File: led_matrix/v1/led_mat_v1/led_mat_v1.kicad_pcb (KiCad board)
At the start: 2 copper layers, 124 parts, among them J1 Left_header, J2 Right_header

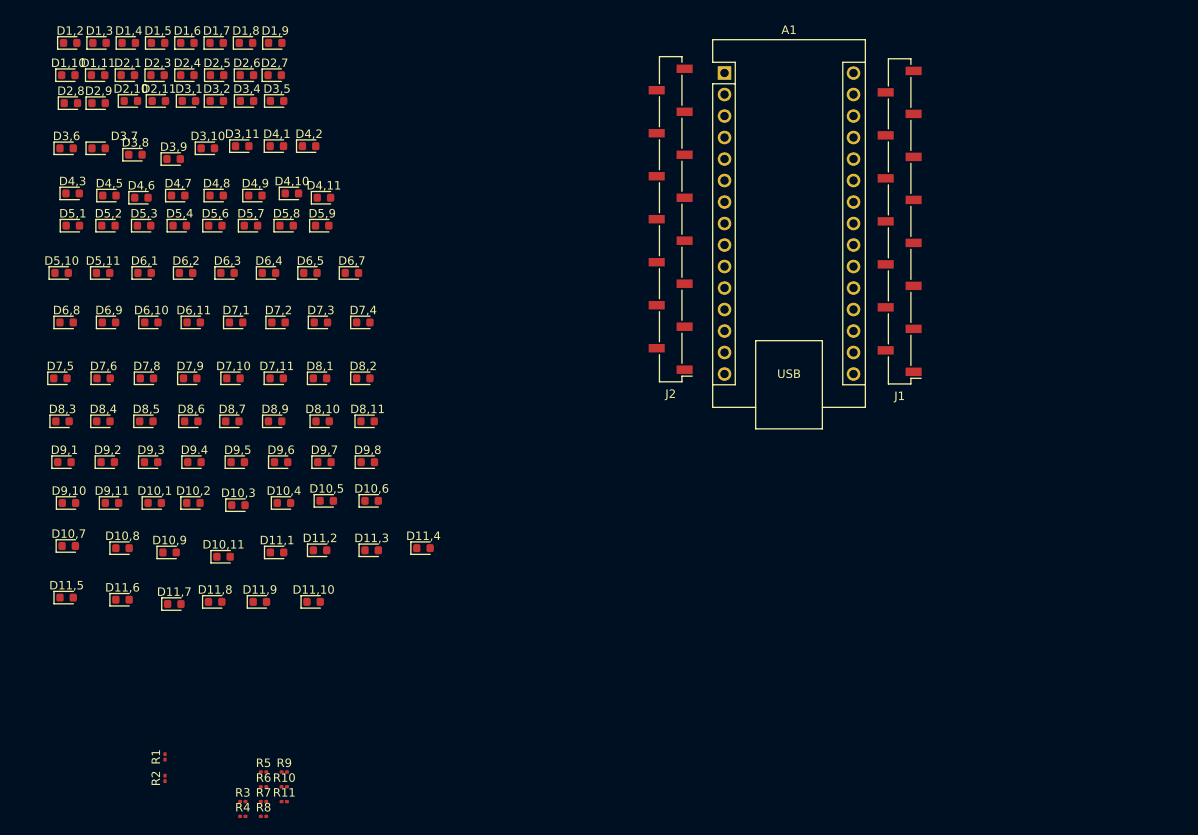
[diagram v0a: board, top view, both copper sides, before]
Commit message: feat(led_matrix): add PCB/schematic exports and update KiCad project files
- Add 3D PCB view export (led_mat_v1.png) and schematic export (led_mat_v1.svg)
- Update schematic, PCB layout, and project files with latest design changes
- Exclude KiCad lock files (*.lck) from version control via .gitignore
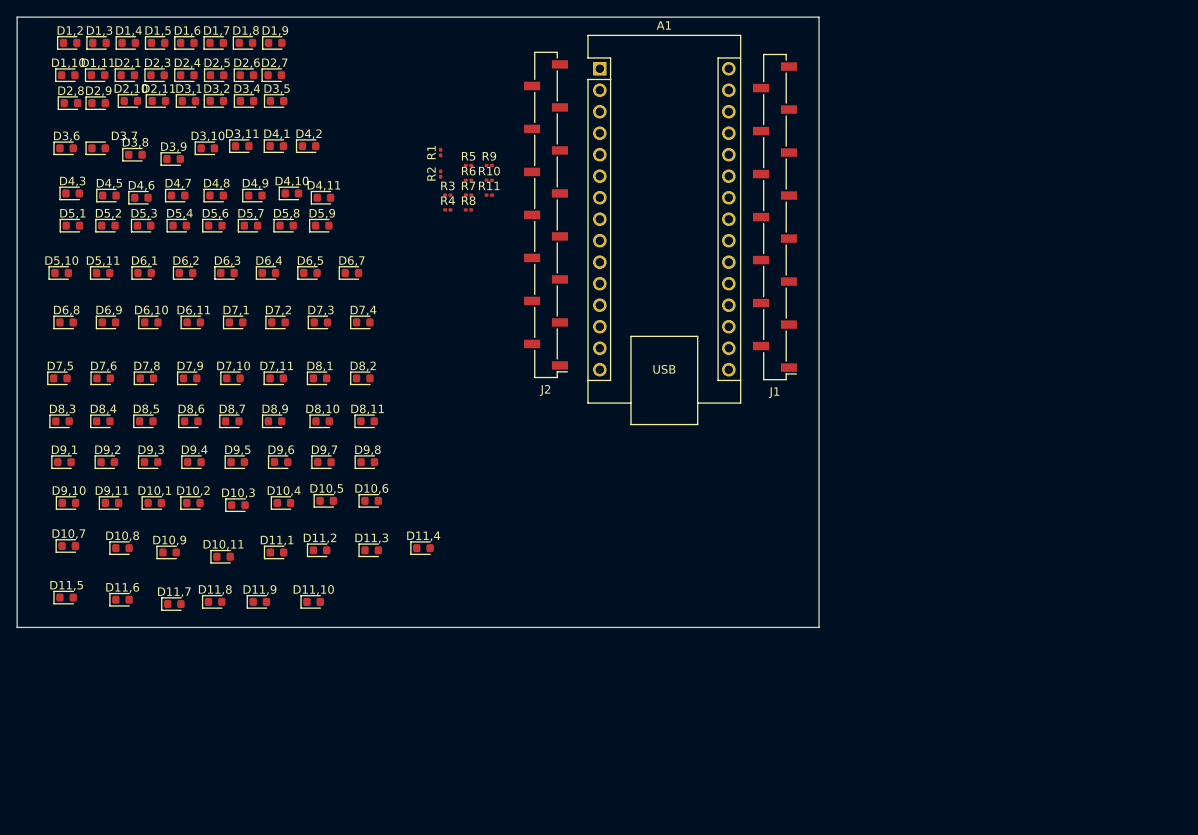
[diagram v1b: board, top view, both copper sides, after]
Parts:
- moved R1 78.5 mm to (105.2, 39.9)
- moved R2 78.5 mm to (105.2, 42.4)
- moved R10 75.6 mm to (110.9, 43.2)
- moved R11 75.6 mm to (110.9, 44.9)
- moved R3 75.6 mm to (106.0, 44.9)
- moved R4 75.6 mm to (106.0, 46.7)
- moved R5 75.6 mm to (108.4, 41.4)
- moved R6 75.6 mm to (108.4, 43.2)
- moved R7 75.6 mm to (108.4, 44.9)
- moved R8 75.6 mm to (108.4, 46.7)
- moved R9 75.6 mm to (110.9, 41.4)
- moved J1 14.7 mm to (144.7, 47.5)
- moved J2 14.7 mm to (117.6, 47.2)
- moved A1 14.7 mm to (124.0, 30.0)
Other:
- board outline added: 94.7 x 72.1 mm
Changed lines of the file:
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@@
 	(footprint "Resistor_SMD:R_0201_0603Metric"
 		(layer "F.Cu")
-		(at 86.68 114.808)
+		(at 110.898 43.152)
 		(descr "Resistor SMD 0201 (0603 Metric), square (rectangular) end terminal, IPC-7351 nominal, (Body size source: https://www.vishay.com/docs/20052/crcw0201e3.pdf)")
 		(tags "resistor")
@@
 	(footprint "Resistor_SMD:R_0201_0603Metric"
 		(layer "F.Cu")
-		(at 84.23 116.558)
+		(at 108.448 44.902)
 		(descr "Resistor SMD 0201 (0603 Metric), square (rectangular) end terminal, IPC-7351 nominal, (Body size source: https://www.vishay.com/docs/20052/crcw0201e3.pdf)")
 		(tags "resistor")
@@
 	(footprint "Connector_PinSocket_2.54mm:PinSocket_1x15_P2.54mm_Vertical_SMD_Pin1Left"
 		(layer "F.Cu")
-		(at 132.334 47.752 180)
+		(at 117.602 47.244 180)
 		(descr "surface-mounted straight socket strip, 1x15, 2.54mm pitch, single row, style 1 (pin 1 left) (https://cdn.harwin.com/pdfs/M20-786.pdf), script generated")
 		(tags "Surface mounted socket strip SMD 1x15 2.54mm single row style1 pin1 left")
@@
 	(footprint "Module:Arduino_Nano"
 		(layer "F.Cu")
-		(at 138.694 30.48)
+		(at 123.962 29.972)
 		(descr "Arduino Nano, http://www.mouser.com/pdfdocs/Gravitech_Arduino_Nano3_0.pdf")
 		(tags "Arduino Nano")
@@
 	(footprint "Resistor_SMD:R_0201_0603Metric"
 		(layer "F.Cu")
-		(at 81.78 116.558)
+		(at 105.998 44.902)
 		(descr "Resistor SMD 0201 (0603 Metric), square (rectangular) end terminal, IPC-7351 nominal, (Body size source: https://www.vishay.com/docs/20052/crcw0201e3.pdf)")
 		(tags "resistor")
@@
 	(footprint "Resistor_SMD:R_0201_0603Metric"
 		(layer "F.Cu")
-		(at 72.589 111.277 90)
+		(at 105.156 39.878 90)
 		(descr "Resistor SMD 0201 (0603 Metric), square (rectangular) end terminal, IPC-7351 nominal, (Body size source: https://www.vishay.com/docs/20052/crcw0201e3.pdf)")
 		(tags "resistor")
@@
 	(footprint "Resistor_SMD:R_0201_0603Metric"
 		(layer "F.Cu")
-		(at 81.78 118.308)
+		(at 105.998 46.652)
 		(descr "Resistor SMD 0201 (0603 Metric), square (rectangular) end terminal, IPC-7351 nominal, (Body size source: https://www.vishay.com/docs/20052/crcw0201e3.pdf)")
 		(tags "resistor")
@@
 	(footprint "Resistor_SMD:R_0201_0603Metric"
 		(layer "F.Cu")
-		(at 72.589 113.817 90)
+		(at 105.156 42.418 90)
 		(descr "Resistor SMD 0201 (0603 Metric), square (rectangular) end terminal, IPC-7351 nominal, (Body size source: https://www.vishay.com/docs/20052/crcw0201e3.pdf)")
 		(tags "resistor")
@@
 	(footprint "Resistor_SMD:R_0201_0603Metric"
 		(layer "F.Cu")
-		(at 84.23 114.808)
+		(at 108.448 43.152)
 		(descr "Resistor SMD 0201 (0603 Metric), square (rectangular) end terminal, IPC-7351 nominal, (Body size source: https://www.vishay.com/docs/20052/crcw0201e3.pdf)")
 		(tags "resistor")
@@
 	(footprint "Resistor_SMD:R_0201_0603Metric"
 		(layer "F.Cu")
-		(at 86.68 113.058)
+		(at 110.898 41.402)
 		(descr "Resistor SMD 0201 (0603 Metric), square (rectangular) end terminal, IPC-7351 nominal, (Body size source: https://www.vishay.com/docs/20052/crcw0201e3.pdf)")
 		(tags "resistor")
@@
 	(footprint "Resistor_SMD:R_0201_0603Metric"
 		(layer "F.Cu")
-		(at 84.23 118.308)
+		(at 108.448 46.652)
 		(descr "Resistor SMD 0201 (0603 Metric), square (rectangular) end terminal, IPC-7351 nominal, (Body size source: https://www.vishay.com/docs/20052/crcw0201e3.pdf)")
 		(tags "resistor")
@@
 	(footprint "Resistor_SMD:R_0201_0603Metric"
 		(layer "F.Cu")
-		(at 86.68 116.558)
+		(at 110.898 44.902)
 		(descr "Resistor SMD 0201 (0603 Metric), square (rectangular) end terminal, IPC-7351 nominal, (Body size source: https://www.vishay.com/docs/20052/crcw0201e3.pdf)")
 		(tags "resistor")
@@
 	(footprint "Resistor_SMD:R_0201_0603Metric"
 		(layer "F.Cu")
-		(at 84.23 113.058)
+		(at 108.448 41.402)
 		(descr "Resistor SMD 0201 (0603 Metric), square (rectangular) end terminal, IPC-7351 nominal, (Body size source: https://www.vishay.com/docs/20052/crcw0201e3.pdf)")
 		(tags "resistor")
@@
 	(footprint "Connector_PinSocket_2.54mm:PinSocket_1x15_P2.54mm_Vertical_SMD_Pin1Left"
 		(layer "F.Cu")
-		(at 159.384 48.006 180)
+		(at 144.652 47.498 180)
 		(descr "surface-mounted straight socket strip, 1x15, 2.54mm pitch, single row, style 1 (pin 1 left) (https://cdn.harwin.com/pdfs/M20-786.pdf), script generated")
 		(tags "Surface mounted socket strip SMD 1x15 2.54mm single row style1 pin1 left")
@@
 		)
 	)
+	(gr_rect
+		(start 55.118 23.876)
+		(end 149.86 95.979596)
+		(stroke
+			(width 0.05)
+			(type default)
+		)
+		(fill no)
+		(locked yes)
+		(layer "Edge.Cuts")
+	)
 	(group ""

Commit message: feat(led_matrix): complete v1 design and add JLCPCB production files
PCB layout and routing finalized. Added gerbers, BOM, and CPL files for
JLCPCB fabrication. Parts ordered. Includes placement helper scripts.
Updated README status to reflect design completion and order placed.
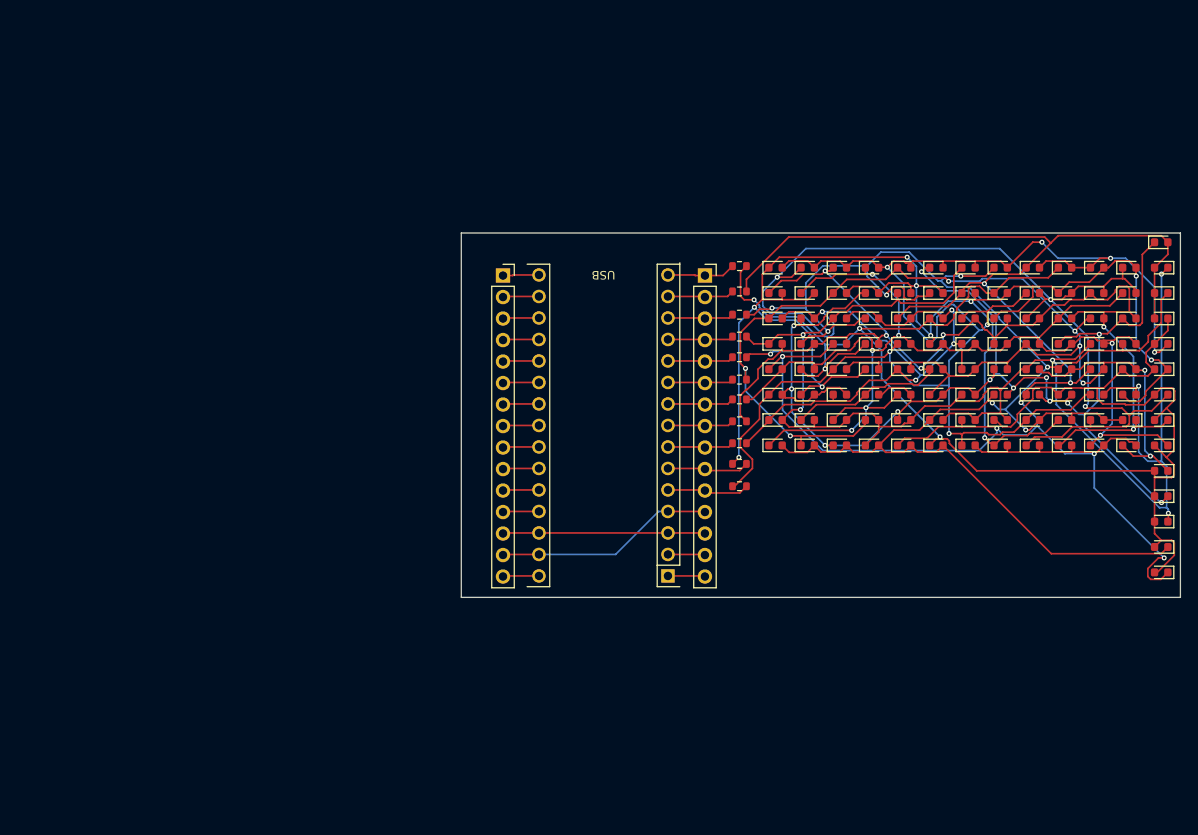
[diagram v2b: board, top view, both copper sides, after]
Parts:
- J1, J2: footprint Connector_PinSocket_2.54mm:PinSocket_1x15_P2.54mm_Vertical_SMD_Pin1Left -> Connector_PinSocket_2.54mm:PinSocket_1x15_P2.54mm_Vertical
- R1, R10, R11, R2, R3, R4, R5, R6, R7, R8, R9: footprint Resistor_SMD:R_0201_0603Metric -> Resistor_SMD:R_0603_1608Metric
- moved D97 134.0 mm to (190.3, 50.5)
- moved D105 130.6 mm to (190.3, 74.5), turned to 180 degrees
- moved D98 127.1 mm to (190.3, 53.5), turned to 180 degrees
- moved D106 123.7 mm to (190.3, 77.5), turned to 180 degrees
- moved D99 121.1 mm to (190.3, 56.5), turned to 180 degrees
- moved D107 117.3 mm to (190.3, 80.5), turned to 180 degrees
- moved D12 117.0 mm to (186.5, 53.5)
- moved D11 116.8 mm to (182.7, 53.5)
- moved D10 116.5 mm to (178.9, 53.5)
- moved D9 116.2 mm to (175.1, 53.5)
- moved D81 114.5 mm to (175.1, 71.5)
- moved D33 114.4 mm to (175.1, 59.5)
- moved D100 114.3 mm to (190.3, 59.5), turned to 180 degrees
- moved D57 114.3 mm to (175.1, 65.5)
- moved D34 113.8 mm to (178.9, 59.5)
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- renumbered D1,2 to D1, D1,11 to D10, D10,11 to D100, D11,1 to D101, D11,2 to D102, D11,3 to D103, D11,4 to D104, D11,5 to D105, D11,6 to D106, D11,7 to D107, D11,8 to D108, D11,9 to D109, D2,1 to D11, D11,10 to D110, D2,3 to D12, D2,4 to D13, D2,5 to D14, D2,6 to D15, D2,7 to D16, D2,8 to D17, D2,9 to D18, D2,10 to D19, D1,3 to D2, D2,11 to D20, D3,1 to D21, D3,2 to D22, D3,4 to D23, D3,5 to D24, D3,6 to D25, D3,7 to D26, D3,8 to D27, D3,9 to D28, D3,10 to D29, D1,4 to D3, D3,11 to D30, D4,1 to D31, D4,2 to D32, D4,3 to D33, D4,5 to D34, D4,6 to D35, D4,7 to D36, D4,8 to D37, D4,9 to D38, D4,10 to D39, D1,5 to D4, D4,11 to D40, D5,1 to D41, D5,2 to D42, D5,3 to D43, D5,4 to D44, D5,6 to D45, D5,7 to D46, D5,8 to D47, D5,9 to D48, D5,10 to D49, D1,6 to D5, D5,11 to D50, D6,1 to D51, D6,2 to D52, D6,3 to D53, D6,4 to D54, D6,5 to D55, D6,7 to D56, D6,8 to D57, D6,9 to D58, D6,10 to D59, D1,7 to D6, D6,11 to D60, D7,1 to D61, D7,2 to D62, D7,3 to D63, D7,4 to D64, D7,5 to D65, D7,6 to D66, D7,8 to D67, D7,9 to D68, D7,10 to D69, D1,8 to D7, D7,11 to D70, D8,1 to D71, D8,2 to D72, D8,3 to D73, D8,4 to D74, D8,5 to D75, D8,6 to D76, D8,7 to D77, D8,9 to D78, D8,10 to D79, D1,9 to D8, D8,11 to D80, D9,1 to D81, D9,2 to D82, D9,3 to D83, D9.4 to D84, D9,5 to D85, D9,6 to D86, D9,7 to D87, D9,8 to D88, D9,10 to D89, D1,10 to D9, D9,11 to D90, D10,1 to D91, D10,2 to D92, D10,3 to D93, D10,4 to D94, D10,5 to D95, D10,6 to D96, D10,7 to D97, D10,8 to D98, D10,9 to D99
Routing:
- net Net-(D100-A): track 0.00 -> 231.6 mm, vias 0 -> 7
- net Net-(D109-K): track 0.00 -> 195.0 mm, vias 0 -> 7
- net Net-(D103-K): track 0.00 -> 188.3 mm, vias 0 -> 7
- net Net-(D10-K): track 0.00 -> 185.8 mm, vias 0 -> 4
- net Net-(D1-K): track 0.00 -> 185.7 mm, vias 0 -> 10
- net Net-(D1-A): track 0.00 -> 179.1 mm, vias 0 -> 7
- net Net-(D108-K): track 0.00 -> 173.3 mm, vias 0 -> 6
- net Net-(D107-K): track 0.00 -> 160.6 mm, vias 0 -> 13
- net Net-(D106-K): track 0.00 -> 153.6 mm, vias 0 -> 8
- net Net-(D104-K): track 0.00 -> 146.3 mm, vias 0 -> 6
- net Net-(D105-K): track 0.00 -> 143.2 mm, vias 0 -> 7
- net GND: track 0.00 -> 26.0 mm
- net /RESET: track 0.00 -> 23.9 mm
- net Row 1: track 0.00 -> 9.75 mm
- net Row 2: track 0.00 -> 9.70 mm
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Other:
- board size 94.7 x 72.1 mm -> 85 x 43.1 mm
